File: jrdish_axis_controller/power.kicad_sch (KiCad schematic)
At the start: 0 parts

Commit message: Updates
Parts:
- added C111, C33: 10uF, PCM_JLCPCB:C_0603, symbol PCM_JLCPCB-Capacitors:0603,10uF,(2)
- added C32: 100nF, PCM_JLCPCB:C_0603, symbol PCM_JLCPCB-Capacitors:0603,100nF
- added C34: 47uF, MyParts:C1206, symbol MyParts:GRM31CR61E476ME44L
- added C35: 1uF, PCM_JLCPCB:C_0402, symbol PCM_JLCPCB-Capacitors:0402,1uF
- added C36: 100nF, MyParts:C0603, symbol MyParts:CC0603KRX7R9BB104
- added C37: 100nF, PCM_JLCPCB:C_0402, symbol PCM_JLCPCB-Capacitors:0402,100nF,(2)
- added C38: 22pF, PCM_JLCPCB:C_0603, symbol PCM_JLCPCB-Capacitors:0603,22pF
- added C39: 22uF, PCM_JLCPCB:C_0805, symbol PCM_JLCPCB-Capacitors:0805,22uF
- added CN2: KF2EDGR-2.54-2P, MyParts:CONN-TH_P2.54_KF2EDGR-2.54-2P, symbol MyParts:KF2EDGR-2.54-2P
- added DC1: DC-005-2.5A-2.0, MyParts:CONN-TH_DC-005-2.5A-2.0, symbol MyParts:DC-005-2.5A-2.0
- added F1: 1812L110/33MR, MyParts:F1812, symbol MyParts:1812L110_33MR
- added L5: 3.3uH, MyParts:IND-SMD_L3.0-W3.0-1, symbol MyParts:ANR3015T4R7M
- added Q1: AO3407A, MyParts:SOT-23-3_L2.9-W1.6-P1.90-LS2.8-BR, symbol MyParts:AO3407A
- added R17: 100kΩ, PCM_JLCPCB:R_0603, symbol PCM_JLCPCB-Resistors:0603,100kΩ
- added R19: 220kΩ, PCM_JLCPCB:R_0603, symbol PCM_JLCPCB-Resistors:0603,220kΩ
- added R20: 10kΩ, PCM_JLCPCB:R_0603, symbol PCM_JLCPCB-Resistors:0603,10kΩ
- added SW1: SS-12F49-G050, MyParts:SW-TH_SS-12F45-GXXX, symbol MyParts:SS-12F49-G050
- added U3: MP2322GQH-Z, MyParts:QFN-8_L2.0-W1.5-P0.50-BL, symbol MyParts:MP2322GQH-Z
- added U4: 976Ω, MyParts:R0603, symbol MyParts:RT0603BRD07976RL
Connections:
- new net: Q1.1 (G), SW1.2
- new net: C38.2, R19.1, U3.5 (FB), U4.1
- new net: C37.1, L5.1, U3.8 (SW)
- new net: C37.2, U3.7 (BST)
- new net: R20.2, SW1.1
- new net: C35.1, R17.2, U3.4 (VCC)
- new net: R17.1, U3.6 (PG)
- new net 12V: C111.1, C32.1, C33.1, CN2.1, Q1.2 (S), U3.2 (IN), U3.3 (EN)
- new net 12V_IN: DC1.1, F1.1
- new net 12V_IN_FUSED: C34.1, C36.1, F1.2, Q1.3 (D), R20.1
- new net 3.3V: C38.1, C39.1, L5.2, U4.2
- new net GND: C111.2, C32.2, C33.2, C34.2, C35.2, C36.2, C39.2, CN2.2, DC1.2, DC1.3, R19.2, SW1.3, U3.1 (GND)
- no-connect marks 0 -> 2
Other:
- note added: "->"
- note added: "1%"
- note added: "1.1A Fuse 33VDC"
- note added: "12V DC input fused to 1.1A max"
- note added: "12V to 3.3V Buck"
- note added: "25V"
- note added: "50V"
- note added: "Circuit to convert 12V DC to 3.3V DC 12V is reverse polatiry and over voltage protected MP2322 used to convert 12V to 3.3V DC 12V DC out will draw max 300mA 3.3V DC out will draw max 300mA 12V available by a output connector: CN1 Buck modeled after John Teel's YouTube video: https://www.youtube.com/watch?v=rLHW4gU6idU and referencing the MP2322 datasheet"
- note added: "From MP2322 Datasheet:"
- note added: "Notes:"
- note added: "Off"
- note added: "On"
- note added: "Only bring out 12V to an external connector"
- note added: "Output"
- note added: "Power Flags"
- note added: "Reverse Voltage Protection P-Channel MOSFET"
- note added: "Switch: In Off pos. Gate is pulled up to 12V, Mosfet is off In On pos. Gate is pulled to Gnd and the Mosfet is on"

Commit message: Passes ERC
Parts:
- L5: LCSC Part C7427087 -> C7427089
- renumbered C34 to C29, C36 to C30, C37 to C31, C111 to C34, C38 to C35, C39 to C36, C35 to C37, CN2 to CN4, R20 to R19, R17 to R20, R19 to R21, SW1 to SW2

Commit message: PCB layout in progress
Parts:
- removed F1: 1812L110/33MR, MyParts:F1812, symbol MyParts:1812L110_33MR
- added F1: 1812L110/48QR, MyParts:F1812, symbol MyParts:1812L110_48QR
- renumbered C29 to C30, C30 to C31, C31 to C32, C32 to C33, C33 to C34, C34 to C35, C35 to C36, C36 to C37, C37 to C38, CN4 to CN5, U4 to R20, R20 to R21, R21 to R22
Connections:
- net 12V_IN: now also F1.1
- net 12V_IN_FUSED: now also F1.2
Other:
- note added: "1.1A Fuse 48VDC"
- note removed: "1.1A Fuse 33VDC"
- company: (none) -> JRSeti

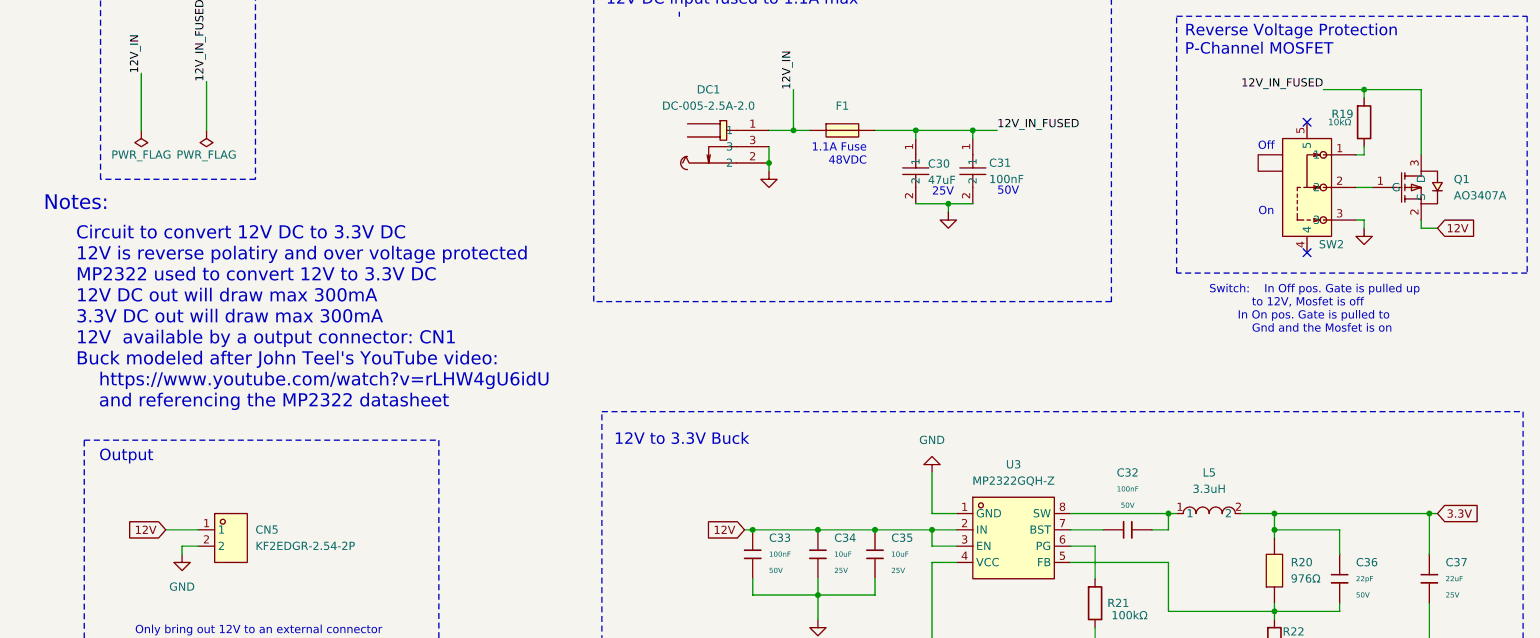
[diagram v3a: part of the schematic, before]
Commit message: New 64pin version - 2 axes
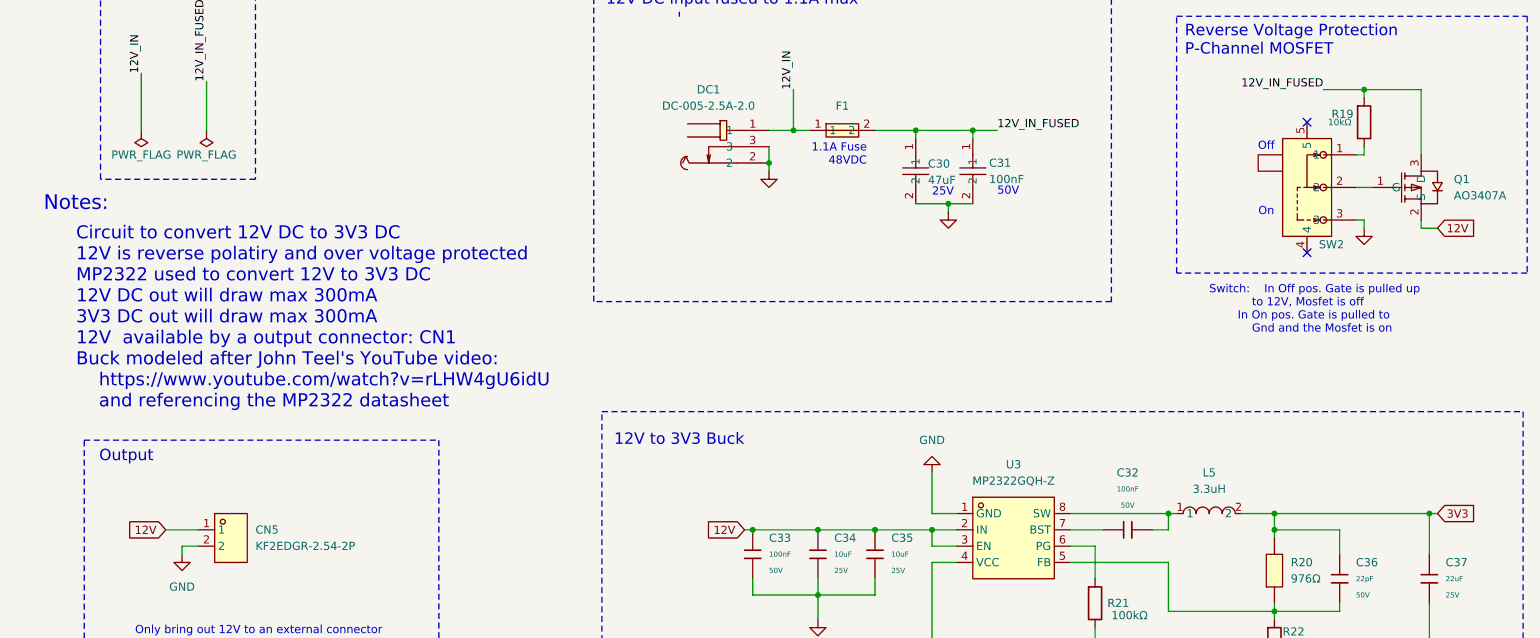
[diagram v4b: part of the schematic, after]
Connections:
- net 3.3V renamed 3V3
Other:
- note added: "12V to 3V3 Buck"
- note added: "Circuit to convert 12V DC to 3V3 DC 12V is reverse polatiry and over voltage protected MP2322 used to convert 12V to 3V3 DC 12V DC out will draw max 300mA 3V3 DC out will draw max 300mA 12V available by a output connector: CN1 Buck modeled after John Teel's YouTube video: https://www.youtube.com/watch?v=rLHW4gU6idU and referencing the MP2322 datasheet"
- note removed: "12V to 3.3V Buck"
- note removed: "Circuit to convert 12V DC to 3.3V DC 12V is reverse polatiry and over voltage protected MP2322 used to convert 12V to 3.3V DC 12V DC out will draw max 300mA 3.3V DC out will draw max 300mA 12V available by a output connector: CN1 Buck modeled after John Teel's YouTube video: https://www.youtube.com/watch?v=rLHW4gU6idU and referencing the MP2322 datasheet"

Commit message: Continuing layout
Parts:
- renumbered C30 to C41, C31 to C42, C32 to C43, C33 to C44, C34 to C45, C35 to C46, C36 to C47, C37 to C48, C38 to C49, CN5 to CN13, L5 to L9, R19 to R20, R20 to R21, R21 to R22, R22 to R23, U3 to U4
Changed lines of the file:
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@@
 		(in_pos_files yes)
 		(dnp no)
-		(property "Reference" "C30"
+		(property "Reference" "C41"
 			(at 160.655 45.847 90)
 			(show_name no)
@@
 			(project "jrdish_axis_controller"
 				(path "/10d7c3e5-be4d-4306-a59e-500b86bd141f/f4424325-c15a-4f12-b98c-68501db44bed"
-					(reference "C30")
+					(reference "C41")
 					(unit 1)
 				)
@@
 		(dnp no)
 		(fields_autoplaced yes)
-		(property "Reference" "C36"
+		(property "Reference" "C47"
 			(at 227.33 107.9499 0)
 			(show_name no)
@@
 			(project "jrdish_axis_controller"
 				(path "/10d7c3e5-be4d-4306-a59e-500b86bd141f/f4424325-c15a-4f12-b98c-68501db44bed"
-					(reference "C36")
+					(reference "C47")
 					(unit 1)
 				)
@@
 		(dnp no)
 		(fields_autoplaced yes)
-		(property "Reference" "CN5"
+		(property "Reference" "CN13"
 			(at 55.88 102.8699 0)
 			(show_name no)
@@
 			(project "jrdish_axis_controller"
 				(path "/10d7c3e5-be4d-4306-a59e-500b86bd141f/f4424325-c15a-4f12-b98c-68501db44bed"
-					(reference "CN5")
+					(reference "CN13")
 					(unit 1)
 				)
@@
 		(in_pos_files yes)
 		(dnp no)
-		(property "Reference" "#FLG05"
+		(property "Reference" "#FLG06"
 			(at 48.26 42.545 0)
 			(hide yes)
@@
 			(project "jrdish_axis_controller"
 				(path "/10d7c3e5-be4d-4306-a59e-500b86bd141f/f4424325-c15a-4f12-b98c-68501db44bed"
-					(reference "#FLG05")
+					(reference "#FLG06")
 					(unit 1)
 				)
@@
 		(in_pos_files yes)
 		(dnp no)
-		(property "Reference" "#FLG04"
+		(property "Reference" "#FLG05"
 			(at 38.1 42.545 0)
 			(hide yes)
@@
 			(project "jrdish_axis_controller"
 				(path "/10d7c3e5-be4d-4306-a59e-500b86bd141f/f4424325-c15a-4f12-b98c-68501db44bed"
-					(reference "#FLG04")
+					(reference "#FLG05")
 					(unit 1)
 				)
@@
 		(dnp no)
 		(fields_autoplaced yes)
-		(property "Reference" "#PWR028"
+		(property "Reference" "#PWR032"
 			(at 228.6 62.23 0)
 			(hide yes)
@@
 			(project "jrdish_axis_controller"
 				(path "/10d7c3e5-be4d-4306-a59e-500b86bd141f/f4424325-c15a-4f12-b98c-68501db44bed"
-					(reference "#PWR028")
+					(reference "#PWR032")
 					(unit 1)
 				)
@@
 		(in_pos_files yes)
 		(dnp no)
-		(property "Reference" "C31"
+		(property "Reference" "C42"
 			(at 170.18 45.72 90)
 			(show_name no)
@@
 			(project "jrdish_axis_controller"
 				(path "/10d7c3e5-be4d-4306-a59e-500b86bd141f/f4424325-c15a-4f12-b98c-68501db44bed"
-					(reference "C31")
+					(reference "C42")
 					(unit 1)
 				)
@@
 		(dnp no)
 		(fields_autoplaced yes)
-		(property "Reference" "#PWR029"
+		(property "Reference" "#PWR033"
 			(at 161.29 87.63 0)
 			(hide yes)
@@
 			(project "jrdish_axis_controller"
 				(path "/10d7c3e5-be4d-4306-a59e-500b86bd141f/f4424325-c15a-4f12-b98c-68501db44bed"
-					(reference "#PWR029")
+					(reference "#PWR033")
 					(unit 1)
 				)
@@
 		(dnp no)
 		(fields_autoplaced yes)
-		(property "Reference" "C32"
+		(property "Reference" "C43"
 			(at 191.77 93.98 90)
 			(show_name no)
@@
 			(project "jrdish_axis_controller"
 				(path "/10d7c3e5-be4d-4306-a59e-500b86bd141f/f4424325-c15a-4f12-b98c-68501db44bed"
-					(reference "C32")
+					(reference "C43")
 					(unit 1)
 				)
@@
 		(dnp no)
 		(fields_autoplaced yes)
-		(property "Reference" "C37"
+		(property "Reference" "C48"
 			(at 241.3 107.9499 0)
 			(show_name no)
@@
 			(project "jrdish_axis_controller"
 				(path "/10d7c3e5-be4d-4306-a59e-500b86bd141f/f4424325-c15a-4f12-b98c-68501db44bed"
-					(reference "C37")
+					(reference "C48")
 					(unit 1)
 				)
@@
 		(dnp no)
 		(fields_autoplaced yes)
-		(property "Reference" "C33"
+		(property "Reference" "C44"
 			(at 135.89 104.1399 0)
 			(show_name no)
@@
 			(project "jrdish_axis_controller"
 				(path "/10d7c3e5-be4d-4306-a59e-500b86bd141f/f4424325-c15a-4f12-b98c-68501db44bed"
-					(reference "C33")
+					(reference "C44")
 					(unit 1)
 				)
@@
 		(dnp no)
 		(fields_autoplaced yes)
-		(property "Reference" "#PWR033"
+		(property "Reference" "#PWR037"
 			(at 161.29 142.24 0)
 			(hide yes)
@@
 			(project "jrdish_axis_controller"
 				(path "/10d7c3e5-be4d-4306-a59e-500b86bd141f/f4424325-c15a-4f12-b98c-68501db44bed"
-					(reference "#PWR033")
+					(reference "#PWR037")
 					(unit 1)
 				)
@@
 		(in_pos_files yes)
 		(dnp no)
-		(property "Reference" "R22"
+		(property "Reference" "R23"
 			(at 215.9 118.745 0)
 			(show_name no)
@@
 			(project "jrdish_axis_controller"
 				(path "/10d7c3e5-be4d-4306-a59e-500b86bd141f/f4424325-c15a-4f12-b98c-68501db44bed"
-					(reference "R22")
+					(reference "R23")
 					(unit 1)
 				)
@@
 		(dnp no)
 		(fields_autoplaced yes)
-		(property "Reference" "C34"
+		(property "Reference" "C45"
 			(at 146.05 104.1399 0)
 			(show_name no)
@@
 			(project "jrdish_axis_controller"
 				(path "/10d7c3e5-be4d-4306-a59e-500b86bd141f/f4424325-c15a-4f12-b98c-68501db44bed"
-					(reference "C34")
+					(reference "C45")
 					(unit 1)
 				)
@@
 		(dnp no)
 		(fields_autoplaced yes)
-		(property "Reference" "L5"
+		(property "Reference" "L9"
 			(at 204.47 93.98 0)
 			(show_name no)
@@
 			(project "jrdish_axis_controller"
 				(path "/10d7c3e5-be4d-4306-a59e-500b86bd141f/f4424325-c15a-4f12-b98c-68501db44bed"
-					(reference "L5")
+					(reference "L9")
 					(unit 1)
 				)
@@
 		(dnp no)
 		(fields_autoplaced yes)
-		(property "Reference" "C35"
+		(property "Reference" "C46"
 			(at 154.94 104.1399 0)
 			(show_name no)
@@
 			(project "jrdish_axis_controller"
 				(path "/10d7c3e5-be4d-4306-a59e-500b86bd141f/f4424325-c15a-4f12-b98c-68501db44bed"
-					(reference "C35")
+					(reference "C46")
 					(unit 1)
 				)
@@
 		(dnp no)
 		(fields_autoplaced yes)
-		(property "Reference" "#PWR031"
+		(property "Reference" "#PWR035"
 			(at 143.51 123.19 0)
 			(hide yes)
@@
 			(project "jrdish_axis_controller"
 				(path "/10d7c3e5-be4d-4306-a59e-500b86bd141f/f4424325-c15a-4f12-b98c-68501db44bed"
-					(reference "#PWR031")
+					(reference "#PWR035")
 					(unit 1)
 				)
@@
 		(dnp no)
 		(fields_autoplaced yes)
-		(property "Reference" "#PWR030"
+		(property "Reference" "#PWR034"
 			(at 44.45 113.03 0)
 			(hide yes)
@@
 			(project "jrdish_axis_controller"
 				(path "/10d7c3e5-be4d-4306-a59e-500b86bd141f/f4424325-c15a-4f12-b98c-68501db44bed"
-					(reference "#PWR030")
+					(reference "#PWR034")
 					(unit 1)
 				)
@@
 		(dnp no)
 		(fields_autoplaced yes)
-		(property "Reference" "#PWR032"
+		(property "Reference" "#PWR036"
 			(at 214.63 133.35 0)
 			(hide yes)
@@
 			(project "jrdish_axis_controller"
 				(path "/10d7c3e5-be4d-4306-a59e-500b86bd141f/f4424325-c15a-4f12-b98c-68501db44bed"
-					(reference "#PWR032")
+					(reference "#PWR036")
 					(unit 1)
 				)
@@
 		(dnp no)
 		(fields_autoplaced yes)
-		(property "Reference" "U3"
+		(property "Reference" "U4"
 			(at 173.99 92.71 0)
 			(show_name no)
@@
 			(project "jrdish_axis_controller"
 				(path "/10d7c3e5-be4d-4306-a59e-500b86bd141f/f4424325-c15a-4f12-b98c-68501db44bed"
-					(reference "U3")
+					(reference "U4")
 					(unit 1)
 				)
@@
 		(dnp no)
 		(fields_autoplaced yes)
-		(property "Reference" "#PWR026"
+		(property "Reference" "#PWR030"
 			(at 135.89 53.34 0)
 			(hide yes)
@@
 			(project "jrdish_axis_controller"
 				(path "/10d7c3e5-be4d-4306-a59e-500b86bd141f/f4424325-c15a-4f12-b98c-68501db44bed"
-					(reference "#PWR026")
+					(reference "#PWR030")
 					(unit 1)
 				)
@@
 		(in_pos_files yes)
 		(dnp no)
-		(property "Reference" "R19"
+		(property "Reference" "R20"
 			(at 223.52 38.1 0)
 			(show_name no)
@@
 			(project "jrdish_axis_controller"
 				(path "/10d7c3e5-be4d-4306-a59e-500b86bd141f/f4424325-c15a-4f12-b98c-68501db44bed"
-					(reference "R19")
+					(reference "R20")
 					(unit 1)
 				)
@@
 		(in_pos_files yes)
 		(dnp no)
-		(property "Reference" "R20"
+		(property "Reference" "R21"
 			(at 217.17 107.9499 90)
 			(show_name no)
@@
 			(project "jrdish_axis_controller"
 				(path "/10d7c3e5-be4d-4306-a59e-500b86bd141f/f4424325-c15a-4f12-b98c-68501db44bed"
-					(reference "R20")
+					(reference "R21")
 					(unit 1)
 				)
@@
 		(in_pos_files yes)
 		(dnp no)
-		(property "Reference" "R21"
+		(property "Reference" "R22"
 			(at 188.595 114.2999 0)
 			(show_name no)
@@
 			(project "jrdish_axis_controller"
 				(path "/10d7c3e5-be4d-4306-a59e-500b86bd141f/f4424325-c15a-4f12-b98c-68501db44bed"
-					(reference "R21")
+					(reference "R22")
 					(unit 1)
 				)
@@
 		(dnp no)
 		(fields_autoplaced yes)
-		(property "Reference" "#PWR027"
+		(property "Reference" "#PWR031"
 			(at 163.83 59.69 0)
 			(hide yes)
@@
 			(project "jrdish_axis_controller"
 				(path "/10d7c3e5-be4d-4306-a59e-500b86bd141f/f4424325-c15a-4f12-b98c-68501db44bed"
-					(reference "#PWR027")
+					(reference "#PWR031")
 					(unit 1)
 				)
@@
 		(dnp no)
 		(fields_autoplaced yes)
-		(property "Reference" "C38"
+		(property "Reference" "C49"
 			(at 163.83 125.7299 0)
 			(show_name no)
@@
 			(project "jrdish_axis_controller"
 				(path "/10d7c3e5-be4d-4306-a59e-500b86bd141f/f4424325-c15a-4f12-b98c-68501db44bed"
-					(reference "C38")
+					(reference "C49")
 					(unit 1)
 				)

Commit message: RS485 isolated areas in place
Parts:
- removed R21: 976Ω, MyParts:R0603, symbol MyParts:RT0603BRD07976RL
- added R21: 976kΩ, Resistor_SMD:R_0805_2012Metric, symbol Device:R
- renumbered C41 to C46, C42 to C47, C43 to C48, C44 to C49, C45 to C50, C46 to C51, C47 to C52, C48 to C53, C49 to C54, CN13 to CN6, L9 to L11
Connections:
- net 12V: now also Q1.3 (D); no longer Q1.2 (S)
- net 12V_IN_FUSED: now also Q1.2 (S); no longer Q1.3 (D)
- net 3V3: now also R21.1
- net at C52.2, R23.1, U4.5 (FB): now also R21.2
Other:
- note added: "0.1%"
- note added: "drain"
- note added: "gate"
- note added: "source"

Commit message: Making refinements
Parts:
- removed C49: 100nF, PCM_JLCPCB:C_0603, symbol PCM_JLCPCB-Capacitors:0603,100nF
- removed C50, C51: 10uF, PCM_JLCPCB:C_0603, symbol PCM_JLCPCB-Capacitors:0603,10uF,(2)
- added C49, C50: 10uF, PCM_JLCPCB:C_0805, symbol PCM_JLCPCB-Capacitors:0805,10uF,(2)
- added C51: 100nF, PCM_JLCPCB:C_0603, symbol PCM_JLCPCB-Capacitors:0603,100nF
- added TP1, TP2, TP3: RH-5016, MyParts:TESTPOINT-SMD_L3.0-W2.0, symbol MyParts:RH-5016
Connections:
- net 12V: now also C49.1, C50.1, C51.1, TP2.1
- net 12V_IN: now also TP1.1
- net 3V3: now also TP3.1
- removed net GND: C46.2, C47.2, C53.2, C54.2, CN6.2, DC1.2, DC1.3, R23.2, SW2.3, U4.1 (GND)
- new net: C46.2, C47.2
- new net: C49.2, C50.2, C51.2
- new net: C53.2, R23.2
- new net: DC1.2, DC1.3
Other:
- note added: "Circuit to convert 12V DC to 3V3 DC 12V is reverse polatiry and over voltage protected MP2322 used to convert 12V to 3V3 DC 12V DC out will draw max 600mA 3V3 DC out will draw max 400mA 12V available by a output connector: CN1 Buck modeled after John Teel's YouTube video: https://www.youtube.com/watch?v=rLHW4gU6idU and referencing the MP2322 datasheet"
- note removed: "Circuit to convert 12V DC to 3V3 DC 12V is reverse polatiry and over voltage protected MP2322 used to convert 12V to 3V3 DC 12V DC out will draw max 300mA 3V3 DC out will draw max 300mA 12V available by a output connector: CN1 Buck modeled after John Teel's YouTube video: https://www.youtube.com/watch?v=rLHW4gU6idU and referencing the MP2322 datasheet"
- title: (none) -> Power
